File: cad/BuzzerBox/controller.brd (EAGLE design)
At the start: 100 x 100 mm, 142 parts, among them J2 RASPBERRYPI-40-PIN-GPIO_PTH_N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, Q1 BSS138, Q2 BSS138, Q3 BSS138, T1 BC849, T10 BC849, T2 BC849, T3 BC849, T4 BC849, T5 BC849, T6 BC849, T7 BC849, T8 BC849, T9 BC849, U1 ATMEGA328P-AU, X1 87758-2616, Y1 16MHz

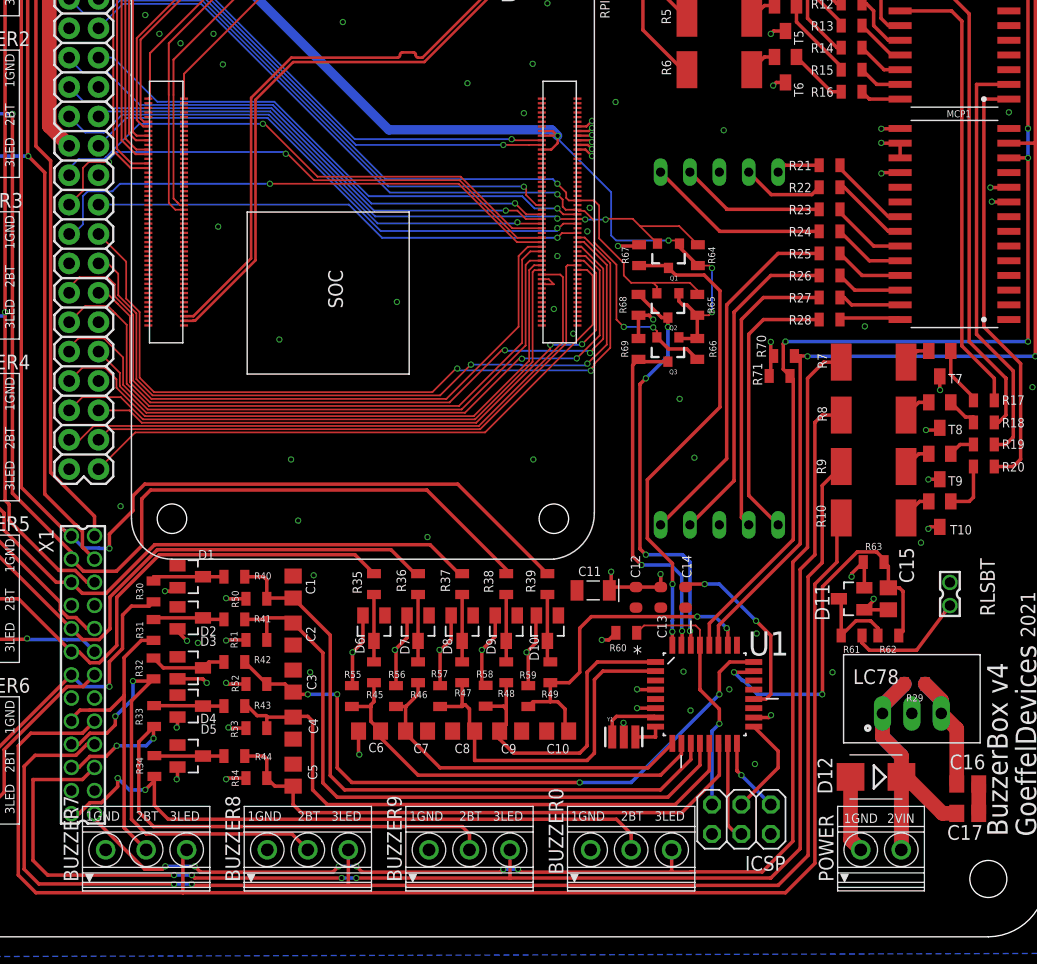
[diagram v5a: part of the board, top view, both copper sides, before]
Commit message: Added leds
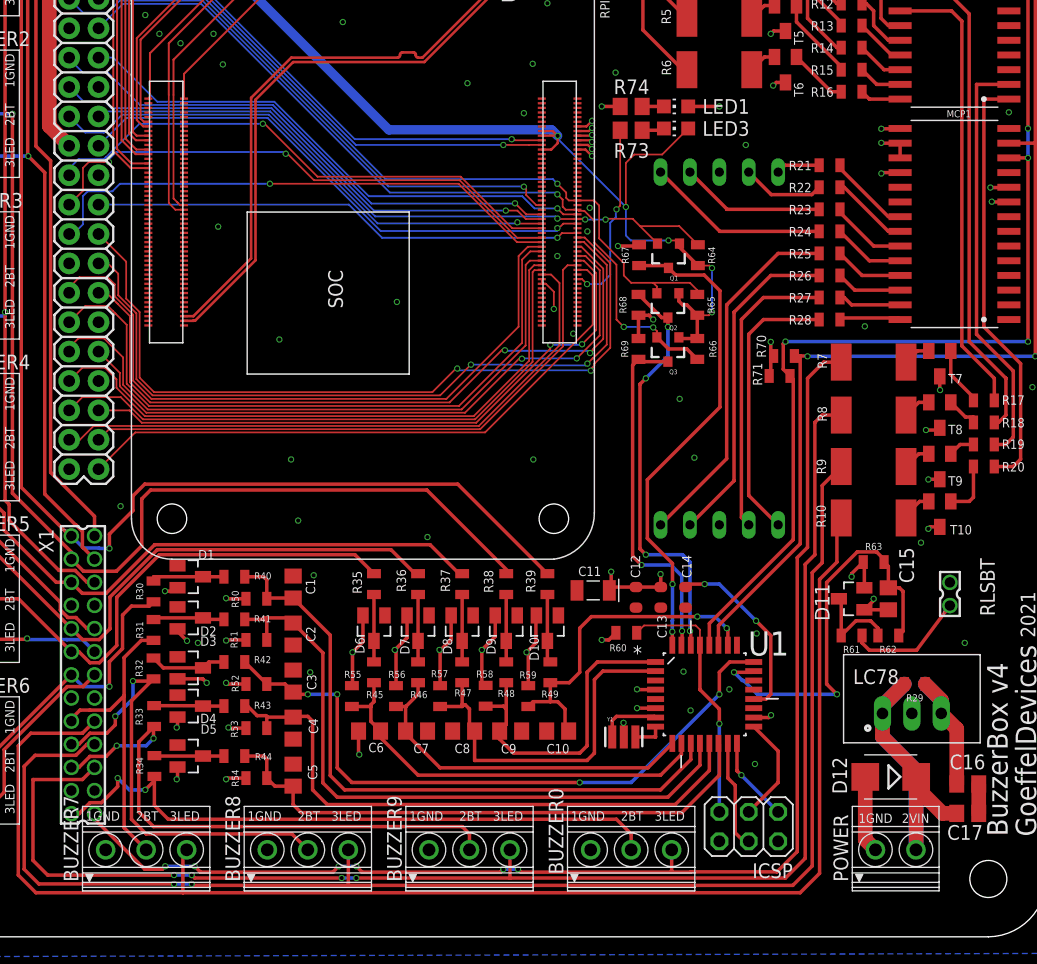
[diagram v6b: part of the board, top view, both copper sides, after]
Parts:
- added LED1: red, led:CHIP-LED0805
- added LED3: green, led:CHIP-LED0805
- added R73, R74: 1k, rcl:R0805
- moved POWER 1.27 mm to (87.0, 7.62)
- moved D12 1.27 mm to (86.6, 13.8)
- moved ICSP 0.90 mm to (74.3, 9.53)
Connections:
- new net N$23: LED3.C, R73.1
- new net N$32: LED1.C, R74.1
- new net N$4: R73.2, RPI-CM4.21
- net +3V3: now also LED3.A
- net +5V: now also LED1.A
- net GND: now also R74.2
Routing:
- net N$4: track 0.00 -> 16.2 mm, vias 0 -> 2
- net +3V3: track 111.5 -> 121.2 mm, vias 5 -> 6
- net +5V: track 119.2 -> 121.9 mm, vias 47 -> 48
- net GND: track 25.8 -> 28.3 mm, vias 49 -> 50
- net N$23: track 0.00 -> 1.94 mm
- net N$32: track 0.00 -> 1.88 mm
- net A0: track 34.3 -> 35.8 mm
- net MOSI: track 8.56 -> 9.46 mm
- net MISO: track 6.49 -> 7.39 mm
- net LED1A1: track 110.6 -> 111.4 mm
- net LED1A0: track 123.1 -> 123.8 mm
- net LED0B0: track 124.0 -> 124.8 mm
- net LED0B1: track 123.0 -> 123.8 mm
- net GP26: track 53.7 -> 53.0 mm

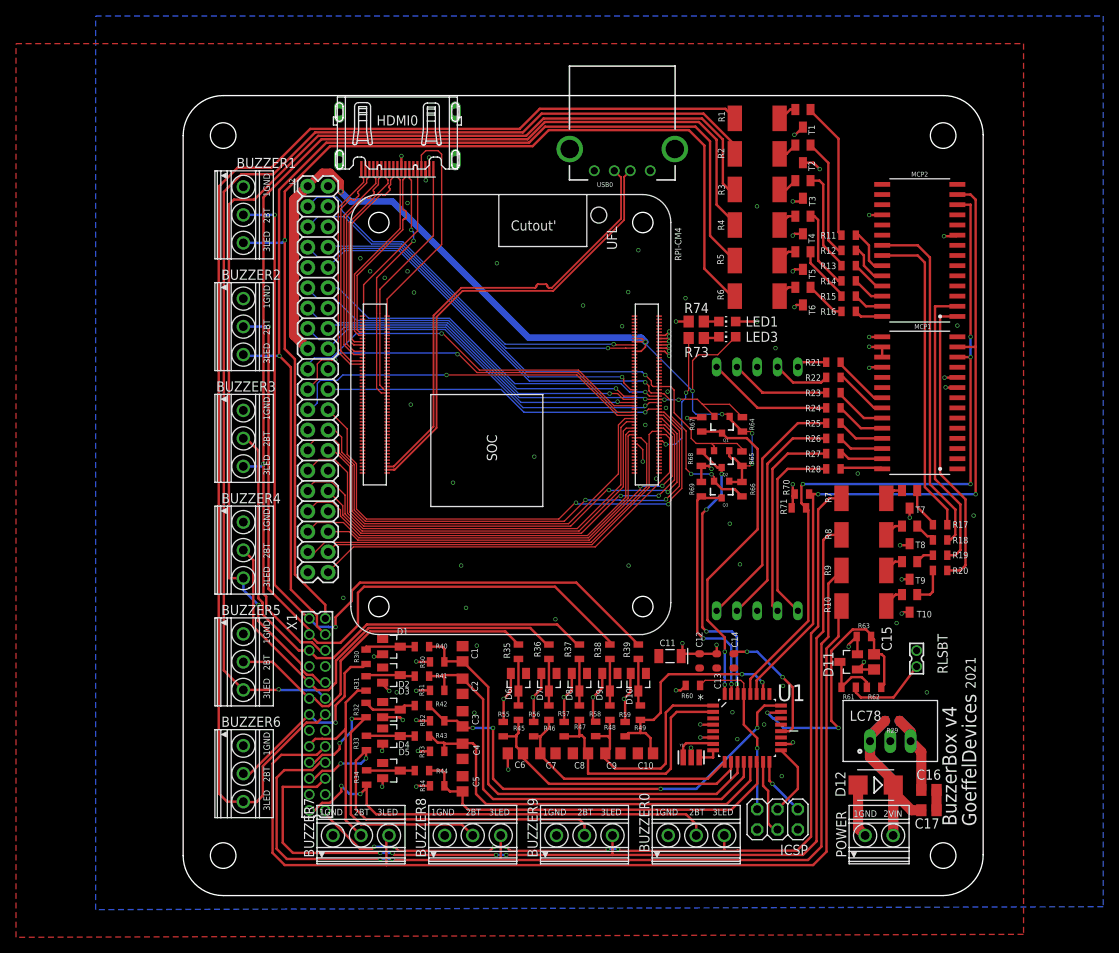
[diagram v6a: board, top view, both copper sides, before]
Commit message: Added ESD protection to USB
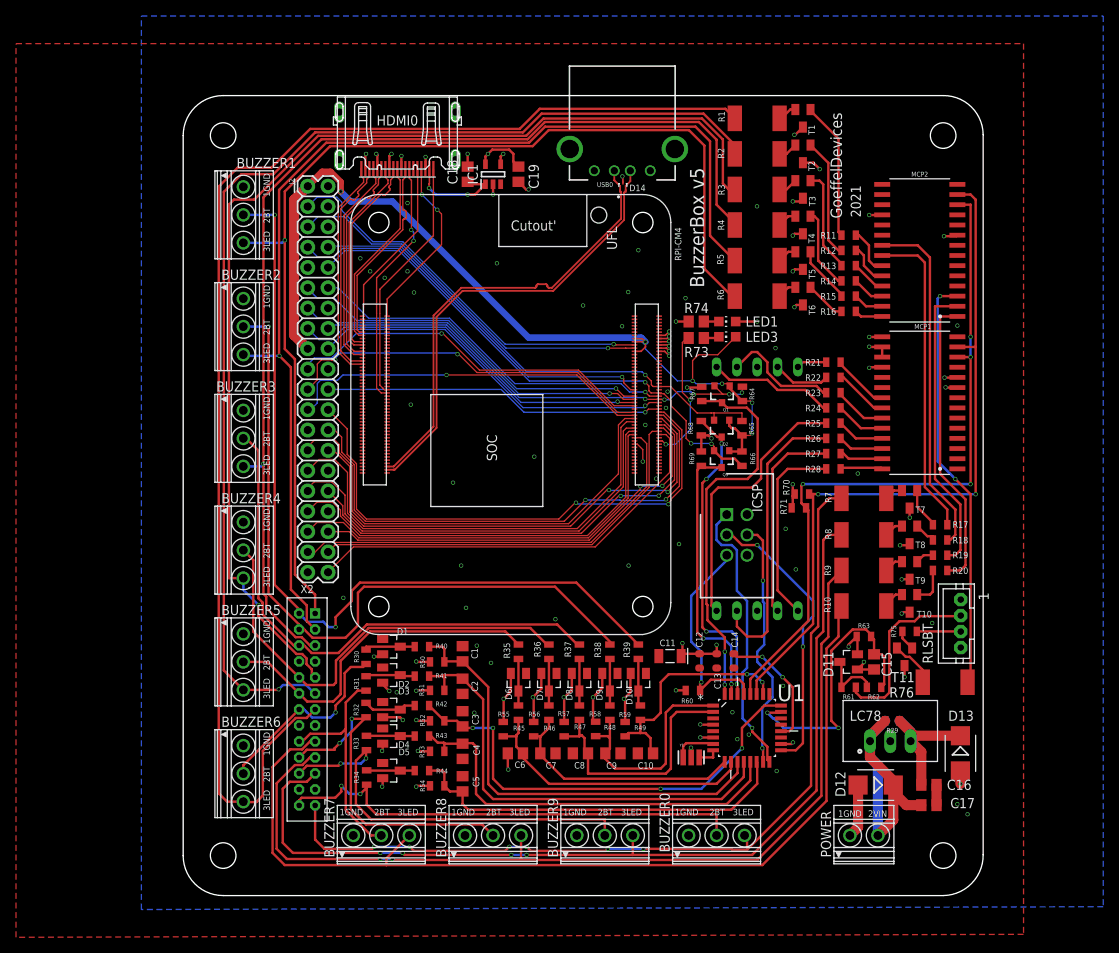
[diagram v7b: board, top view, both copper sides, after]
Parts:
- removed X1: 87758-2616, con-molex:87758-2616
- added C18, C19: 100nF, rcl:C0805
- added D13: (no value), diode:SMB
- added D14: TPD2EUSB30DRTR, TPD2EUSB30DRTR:SOTFL35P100X50-3N
- added IC1: TPS2041CDBVT, SamacSys_Parts:SOT95P280X145-5N
- added R75: 1K, SparkFun-Resistors:0805
- added R76: 50, rcl:R2512
- added T11: BC849, transistor:SOT23
- added X2: B26B-PHDSS, con-JST PHD:B26B-PHDSS
- ICSP: value (none) -> 61200621621; device Connettori:2X03 -> SamacSys_Parts:SHDR6W64P254_2X3_1528X910X910P
- RLSBT: value 87758-0216 -> (none); device con-molex:87758-0216 -> jst-ph:JST-PH4
- moved ICSP 38.6 mm to (67.9, 47.6), turned to 270 degrees
- moved RLSBT 7.04 mm to (97.2, 34.0), turned to 90 degrees
- moved Q1 3.81 mm to (67.4, 62.7)
- moved Q2 3.81 mm to (67.3, 58.4)
- moved Q3 3.81 mm to (67.3, 54.6)
- moved R64 3.81 mm to (69.9, 62.7)
- moved R65 3.81 mm to (69.8, 58.4)
- moved R66 3.81 mm to (69.8, 54.6)
- moved R67 3.81 mm to (64.8, 62.7)
- moved R68 3.81 mm to (64.8, 58.4)
- moved R69 3.81 mm to (64.8, 54.6)
- moved BUZZER7 2.54 mm to (24.8, 7.62)
- moved BUZZER8 2.54 mm to (38.7, 7.62)
- moved BUZZER9 2.54 mm to (52.7, 7.62)
- moved BUZZER0 2.54 mm to (66.7, 7.62)
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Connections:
- new net 5VHDMI: C18.1, HDMI0.P$18, IC1.1
- new net N$35: R75.2, T11.1
- new net N$36: R76.2, T11.2
- new net N$37: R75.1, RLSBT.3
- new net RLBTLED: MCP2.3, R76.1
- net +5V: now also C19.1, D13.C, IC1.4, IC1.5, T11.3; no longer HDMI0.P$18
- net BUZZ0: now also X2.26; no longer X1.25
- net BUZZ1: now also X2.2; no longer X1.1
- net BUZZ2: now also X2.4; no longer X1.3
- net BUZZ3: now also X2.6; no longer X1.5
- net BUZZ4: now also X2.10; no longer X1.9
- net BUZZ5: now also X2.12; no longer X1.11
- net BUZZ6: now also X2.14; no longer X1.13
- net BUZZ7: now also X2.18; no longer X1.17
- net BUZZ8: now also X2.20; no longer X1.19
- net BUZZ9: now also X2.22; no longer X1.21
- net GND: now also C18.2, C19.2, D13.A, D14.3, IC1.2, RLSBT.1, RLSBT.4, X2.15, X2.16, X2.23, X2.24, X2.7, X2.8; no longer RLSBT.2, X1.15, X1.16, X1.23, X1.24, X1.7, X1.8
- net LED0A2: now also X2.13; no longer X1.14
- net LED0A3: now also X2.11; no longer X1.12
- net LED0A4: now also X2.9; no longer X1.10
- net LED0B0: now also X2.17; no longer X1.18
- net LED0B1: now also X2.19; no longer X1.20
- net LED1A0: now also X2.21; no longer X1.22
- net LED1A1: now also X2.25; no longer X1.26
- net LED1A5: now also X2.5; no longer X1.6
- net LED1A6: now also X2.3; no longer X1.4
- net LED1A7: now also X2.1; no longer X1.2
- net RLSBT: now also RLSBT.2; no longer RLSBT.1
- net USB_N: now also D14.2
- net USB_P: now also D14.1
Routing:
- net RLBTLED: track 0.00 -> 52.4 mm, vias 0 -> 2
- net MISO: track 7.39 -> 35.4 mm
- net SCK: track 9.29 -> 35.6 mm, vias 0 -> 2
- net MOSI: track 9.46 -> 31.7 mm, vias 0 -> 2
- net +5V: track 121.9 -> 135.9 mm, vias 48 -> 50
- net GND: track 28.3 -> 41.0 mm, vias 50 -> 60
- net 5VHDMI: track 0.00 -> 12.7 mm, vias 0 -> 2
- net RLSBT: track 10.4 -> 22.7 mm
- net C: track 28.6 -> 36.2 mm
- net D2: track 42.0 -> 48.2 mm
- net N$36: track 0.00 -> 5.90 mm
- net N$37: track 0.00 -> 5.50 mm
- net HDMI_SDA: track 27.7 -> 22.3 mm, vias 0 -> 2
- net LED0B1: track 123.8 -> 118.6 mm
- net LED1A0: track 123.8 -> 118.9 mm
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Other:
- board text added: "BuzzerBox v5"
- board text removed: "BuzzerBox v4"

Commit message: Added PE to XLR Board
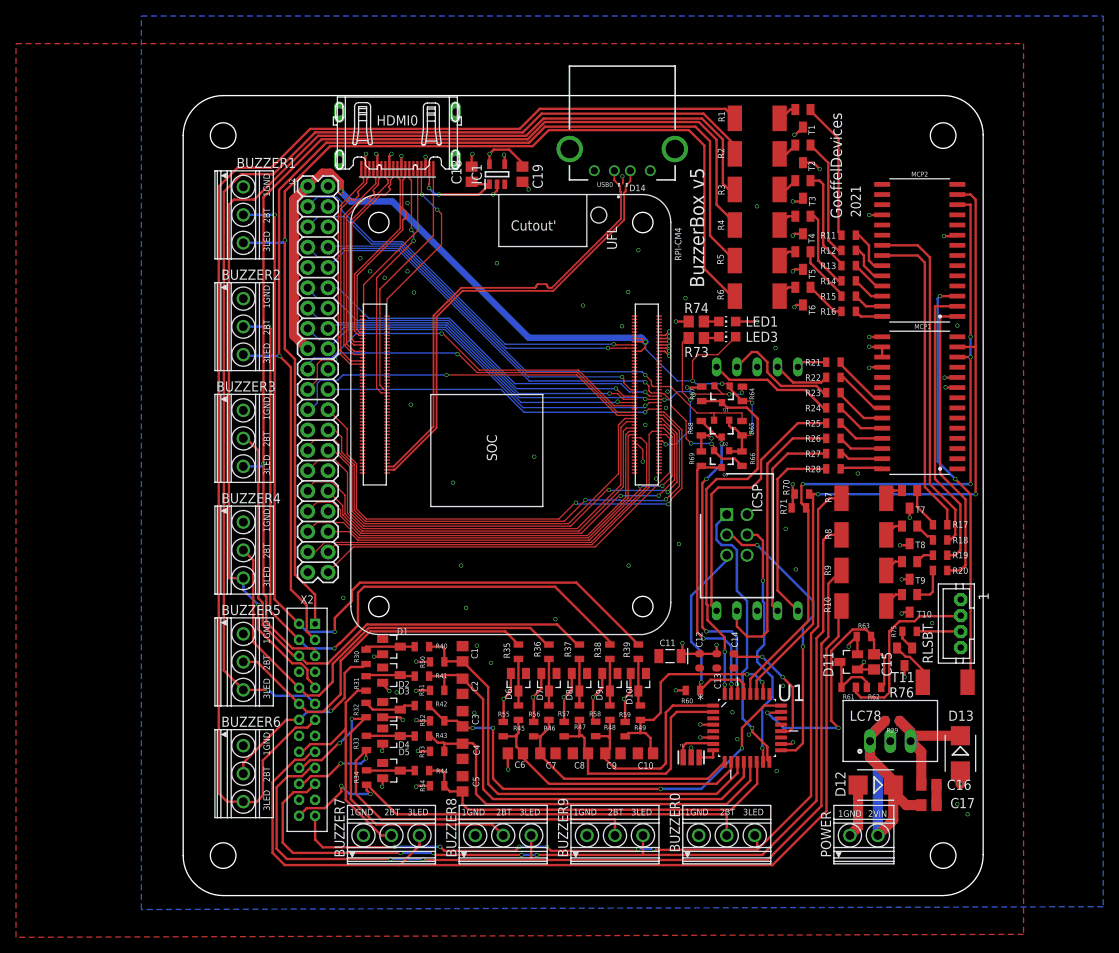
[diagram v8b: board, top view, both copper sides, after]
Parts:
- moved X2 1.30 mm to (15.5, 22.0)
- moved BUZZER8 1.27 mm to (40.0, 7.62)
- moved BUZZER9 1.27 mm to (54.0, 7.62)
- moved BUZZER7 1.27 mm to (26.0, 7.62)
- moved BUZZER0 1.27 mm to (67.9, 7.62)
- moved C18 0.50 mm to (36.1, 90.2)
- moved C19 0.50 mm to (42.4, 90.2)
- moved IC1 0.50 mm to (39.2, 90.2)
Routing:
- net LED1A5: track 135.4 -> 137.4 mm
- net BUZZ2: track 90.5 -> 92.3 mm, vias 1 -> 2
- net BUZZ3: track 67.3 -> 69.2 mm
- net BUZZ1: track 105.1 -> 106.6 mm
- net BUZZ4: track 55.8 -> 57.4 mm
- net LED0A4: track 139.7 -> 141.2 mm
- net LED1A6: track 135.5 -> 136.8 mm
- net LED1A7: track 136.7 -> 138.0 mm
- net LED0A2: track 165.4 -> 164.2 mm
- net BUZZ0: track 60.7 -> 61.9 mm
- net LED0B0: track 120.8 -> 119.7 mm
- net BUZZ5: track 43.2 -> 44.3 mm
- net BUZZ9: track 51.4 -> 52.5 mm
- net BUZZ7: track 28.8 -> 29.9 mm
- net BUZZ6: track 24.7 -> 23.6 mm
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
